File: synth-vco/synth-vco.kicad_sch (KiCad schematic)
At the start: 146 parts, among them J1 Conn_Coaxial, J2 Screw_Terminal_01x10, J3 Screw_Terminal_01x05, J4 Conn_Coaxial, J5 Barrel_Jack, U1 ADF4158, U10 LT3045IMSE_TRPBF, U11 LT3045IMSE_TRPBF, U12 LT3045IMSE_TRPBF, U13 LT8570EMS8E_TRPBF, U14 LT3065EDDPBF, U15 LT3065EDDPBF, U16 BT09E, U3 ADP-2-10+, U4 DAT-15R5A-SP+, U5 OPA192IDGKT, U6 TPSM53602RDAR, U7 LT3045IMSE_TRPBF, U8 LT3045IMSE_TRPBF, U9 LT3045IMSE_TRPBF, Y3 CVCO55CW-0500-1000

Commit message: fix: resistors, capacitors and inductors footprints
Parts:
- C1, C12, C13, C14, C15, C16, C17, C2, C20, C21, C22, C4, C5, C66, C67, C68, C69, C71, C72: footprint (none) -> Capacitor_SMD:C_0603_1608Metric_Pad1.08x0.95mm_HandSolder
- C23, C24, C29, C30, C31, C32, C33, C34, C35, C36, C38, C39, C41, C42, C44: footprint Capacitor_SMD:C_0603_1608Metric_Pad1.08x0.95mm_HandSolder -> Capacitor_SMD:C_0805_2012Metric_Pad1.18x1.45mm_HandSolder
- C25, C26, C27, C28, C49, C51, C55, C65: footprint Capacitor_SMD:C_0603_1608Metric_Pad1.08x0.95mm_HandSolder -> Capacitor_SMD:C_1206_3216Metric_Pad1.33x1.80mm_HandSolder
- C56: footprint Capacitor_SMD:C_0201_0603Metric_Pad0.64x0.40mm_HandSolder -> Capacitor_SMD:C_0603_1608Metric_Pad1.08x0.95mm_HandSolder
- C6, C7: footprint Capacitor_SMD:C_0201_0603Metric_Pad0.64x0.40mm_HandSolder -> Capacitor_SMD:C_1206_3216Metric_Pad1.33x1.80mm_HandSolder
- C70: footprint (none) -> Capacitor_SMD:C_0805_2012Metric_Pad1.18x1.45mm_HandSolder
- C9: footprint (none) -> Capacitor_SMD:C_1206_3216Metric_Pad1.33x1.80mm_HandSolder
- L1, L3, L4, L5, L6: footprint Inductor_SMD:L_0201_0603Metric_Pad0.64x0.40mm_HandSolder -> Inductor_SMD:L_0603_1608Metric_Pad1.05x0.95mm_HandSolder
- R1, R2, R22, R23, R24, R25, R26, R27, R28, R29, R30, R31, R32, R33, R34, R35, R36, R37, R38, R4: footprint Resistor_SMD:R_0201_0603Metric_Pad0.64x0.40mm_HandSolder -> Resistor_SMD:R_0603_1608Metric_Pad0.98x0.95mm_HandSolder
- R10, R11, R12, R13, R14, R15, R16, R17, R18, R19, R20, R21, R3, R39, R40, R41, R5, R6, R8, R9: footprint Resistor_SMD:R_01005_0402Metric_Pad0.57x0.30mm_HandSolder -> Resistor_SMD:R_0603_1608Metric_Pad0.98x0.95mm_HandSolder
- R7: footprint (none) -> Resistor_SMD:R_0603_1608Metric_Pad0.98x0.95mm_HandSolder

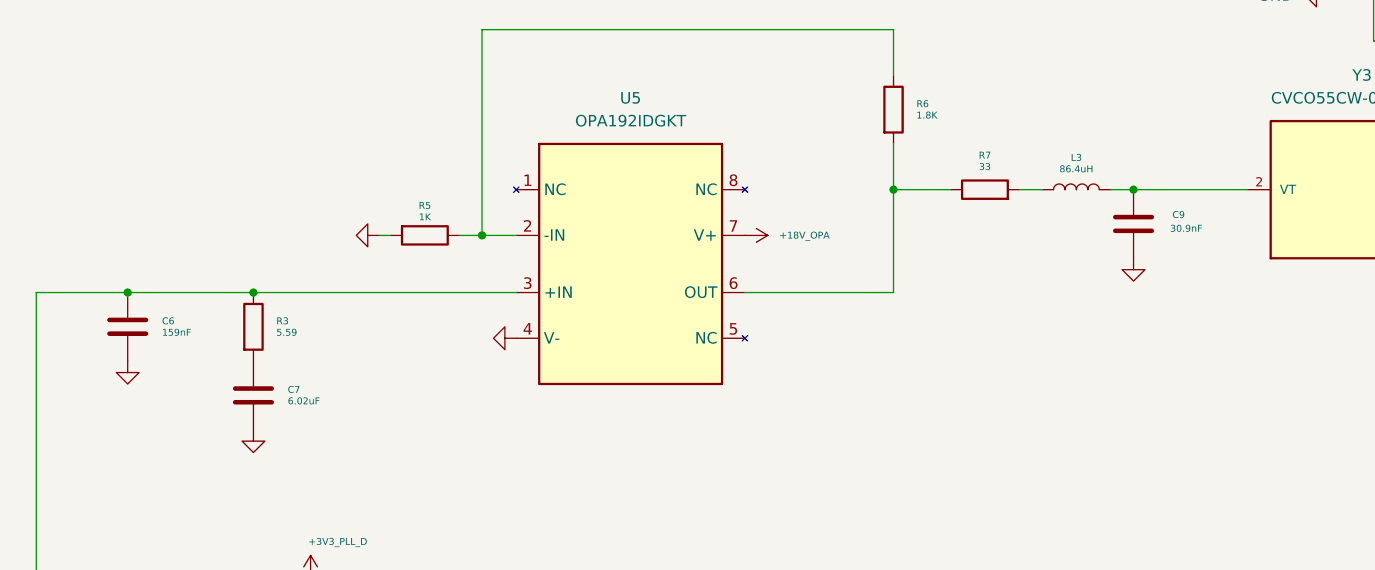
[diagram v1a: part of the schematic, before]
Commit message: refactor: standard values for adf-vco loop components
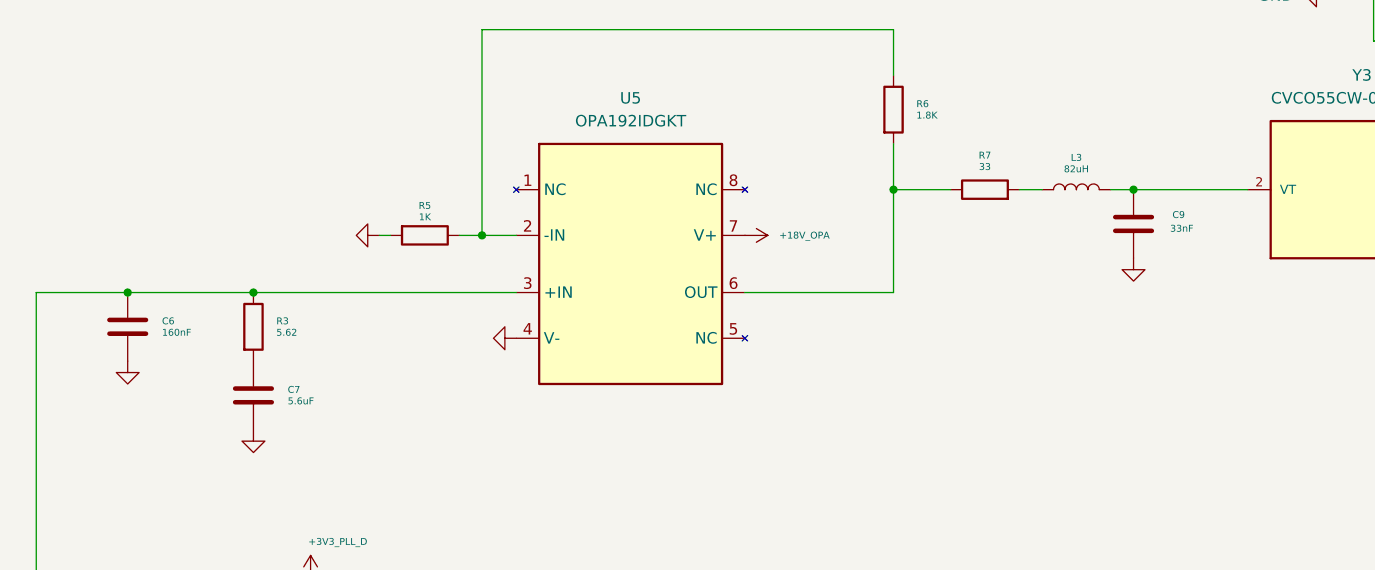
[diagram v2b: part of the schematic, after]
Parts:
- C6: value 159nF -> 160nF
- C7: value 6.02uF -> 5.6uF
- C9: value 30.9nF -> 33nF
- L3: value 86.4uH -> 82uH
- R3: value 5.59 -> 5.62
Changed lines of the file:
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@@
 			)
 		)
-		(property "Value" "30.9nF"
+		(property "Value" "33nF"
 			(at 334.264 324.358 0)
 			(show_name no)
@@
 			)
 		)
-		(property "Value" "6.02uF"
+		(property "Value" "5.6uF"
 			(at 236.22 343.535 0)
 			(show_name no)
@@
 			)
 		)
-		(property "Value" "86.4uH"
+		(property "Value" "82uH"
 			(at 323.85 317.754 90)
 			(show_name no)
@@
 			)
 		)
-		(property "Value" "5.59"
+		(property "Value" "5.62"
 			(at 234.95 335.915 0)
 			(show_name no)
@@
 			)
 		)
-		(property "Value" "159nF"
+		(property "Value" "160nF"
 			(at 222.25 335.915 0)
 			(show_name no)

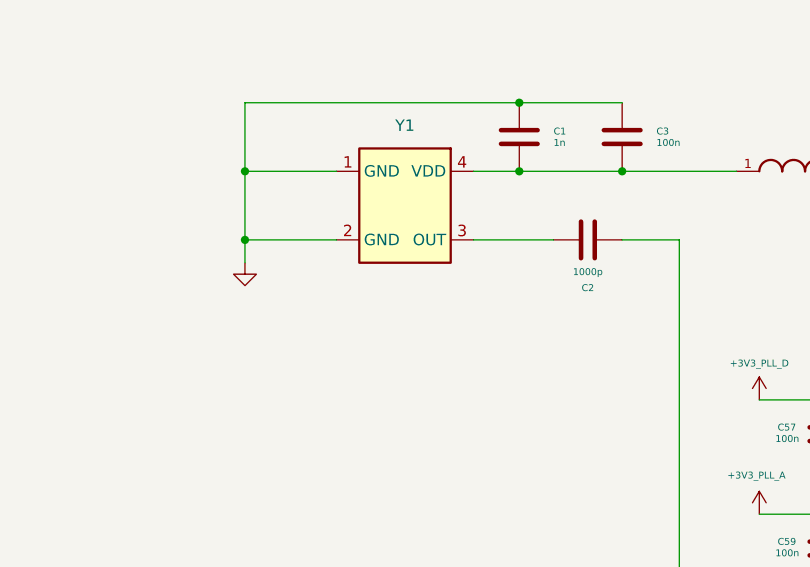
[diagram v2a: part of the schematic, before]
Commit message: fix: added value field for ft3mn
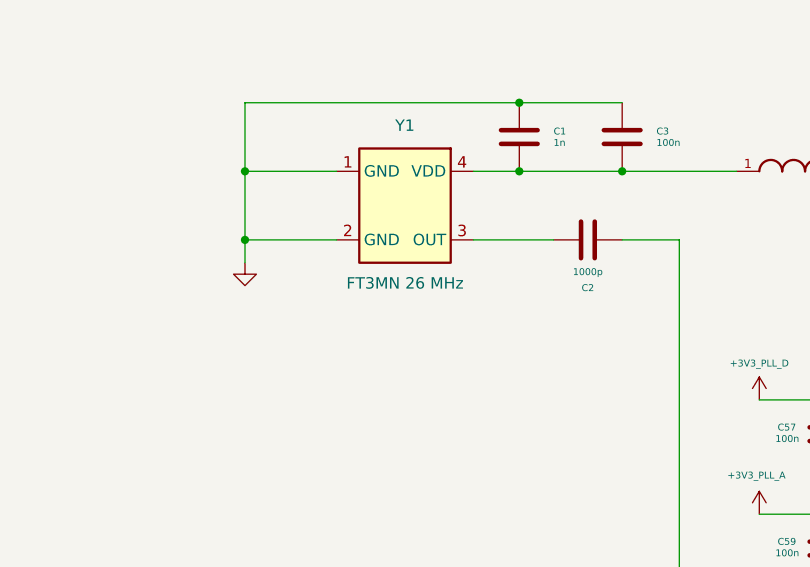
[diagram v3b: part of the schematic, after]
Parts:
- Y1: value (none) -> FT3MN 26 MHz
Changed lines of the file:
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@@
 		(in_pos_files yes)
 		(dnp no)
-		(fields_autoplaced yes)
 		(property "Reference" "Y1"
 			(at 110.49 299.72 90)
@@
 			)
 		)
-		(property "Value" ""
-			(at 110.49 308.61 0)
+		(property "Value" "FT3MN 26 MHz"
+			(at 110.49 317.246 90)
 			(show_name no)
 			(do_not_autoplace no)

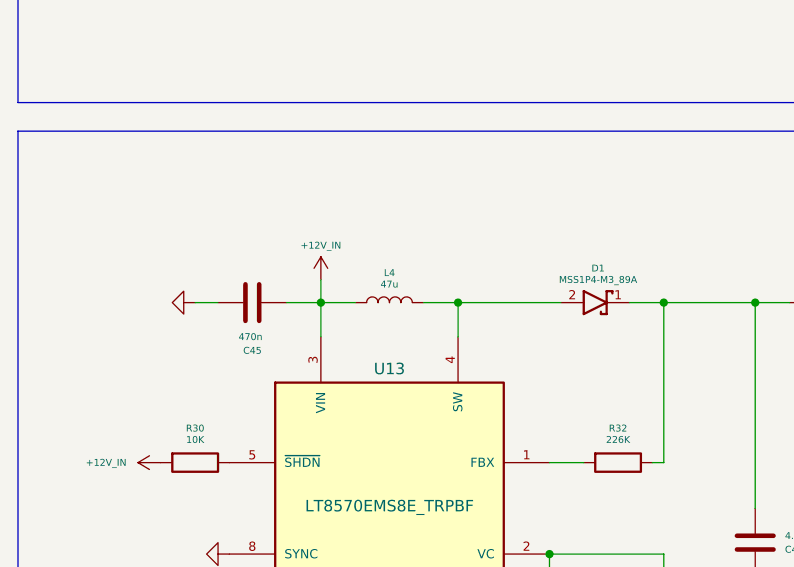
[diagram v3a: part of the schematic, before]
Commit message: fix: switched the regular boost inductor for wurth's LQS-4018
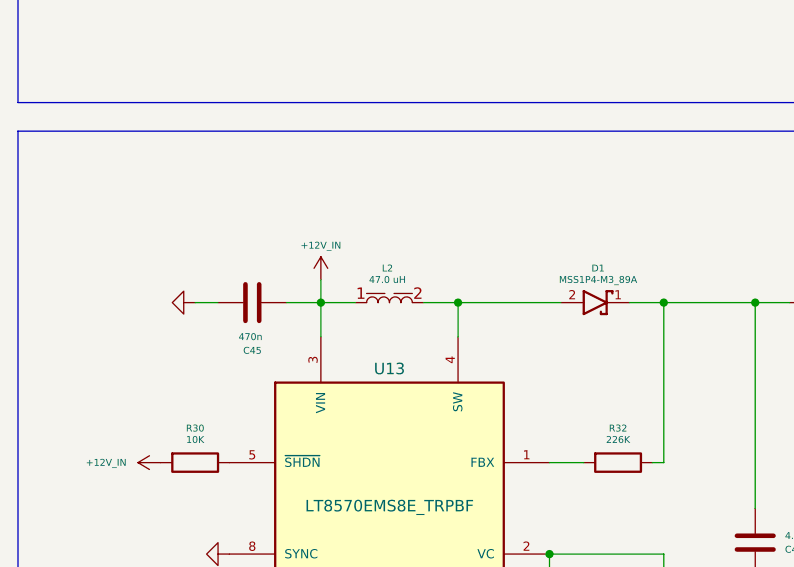
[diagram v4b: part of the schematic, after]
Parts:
- removed L4: 47u, Inductor_SMD:L_0603_1608Metric_Pad1.05x0.95mm_HandSolder, symbol Device:L
- added L2: 47.0 uH, GPR_Radar_Footprints:L_Wurth_WE-LQS-4018, symbol Inductor_Wurth_WE-LQS:4018_74404042470
- L3: footprint Inductor_SMD:L_0603_1608Metric_Pad1.05x0.95mm_HandSolder -> Inductor_SMD:L_0805_2012Metric_Pad1.05x1.20mm_HandSolder
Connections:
- net +12V_IN: now also L2.1
- net at D1.2, U13.4 (SW): now also L2.2
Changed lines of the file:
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@@
 	)
 	(symbol
-		(lib_id "Device:L")
-		(at 69.85 138.43 90)
-		(unit 1)
-		(body_style 1)
-		(exclude_from_sim no)
-		(in_bom yes)
-		(on_board yes)
-		(in_pos_files yes)
-		(dnp no)
-		(property "Reference" "L4"
-			(at 69.85 135.128 90)
-			(show_name no)
-			(do_not_autoplace no)
-			(effects
-				(font
-					(size 0.762 0.762)
-				)
-			)
-		)
-		(property "Value" "47u"
-			(at 69.85 136.398 90)
-			(show_name no)
-			(do_not_autoplace no)
-			(effects
-				(font
-					(size 0.762 0.762)
-				)
-			)
-		)
-		(property "Footprint" "Inductor_SMD:L_0603_1608Metric_Pad1.05x0.95mm_HandSolder"
-			(at 69.85 138.43 0)
-			(hide yes)
-			(show_name no)
-			(do_not_autoplace no)
-			(effects
-				(font
-					(size 1.27 1.27)
-				)
-			)
-		)
-		(property "Datasheet" ""
-			(at 69.85 138.43 0)
-			(hide yes)
-			(show_name no)
-			(do_not_autoplace no)
-			(effects
-				(font
-					(size 1.27 1.27)
-				)
-			)
-		)
-		(property "Description" "Inductor"
-			(at 69.85 138.43 0)
-			(hide yes)
-			(show_name no)
-			(do_not_autoplace no)
-			(effects
-				(font
-					(size 1.27 1.27)
-				)
-			)
-		)
-		(pin "2"
-		)
-		(pin "1"
-		)
-		(instances
-			(project "synth-vco"
-				(path "/73cd0915-f93d-4399-bfe5-6d917fa8cde7"
-					(reference "L4")
-					(unit 1)
-				)
-			)
-		)
-	)
-	(symbol
 		(lib_id "power:GND")
 		(at 52.07 166.37 270)
@@
 			)
 		)
-		(property "Footprint" "Inductor_SMD:L_0603_1608Metric_Pad1.05x0.95mm_HandSolder"
+		(property "Footprint" "Inductor_SMD:L_0805_2012Metric_Pad1.05x1.20mm_HandSolder"
 			(at 323.85 320.04 0)
 			(hide yes)
@@
 					(unit 1)
 				)
+			)
+		)
+	)
+	(symbol
+		(lib_id "Inductor_Wurth_WE-LQS:4018_74404042470")
+		(at 69.85 138.43 0)
+		(unit 1)
+		(body_style 1)
+		(exclude_from_sim no)
+		(in_bom yes)
+		(on_board yes)
+		(in_pos_files yes)
+		(dnp no)
+		(fields_autoplaced yes)
+		(property "Reference" "L2"
+			(at 69.6277 134.62 0)
+			(show_name no)
+			(do_not_autoplace no)
+			(effects
+				(font
+					(size 0.762 0.762)
+				)
+			)
+		)
+		(property "Value" "47.0 uH"
+			(at 82.55 115.57 0)
+			(hide yes)
+			(show_name no)
+			(do_not_autoplace no)
+			(effects
+				(font
+					(size 1.27 1.27)
+				)
+				(justify left)
+			)
+		)
+		(property "Footprint" "GPR_Radar_Footprints:L_Wurth_WE-LQS-4018"
+			(at 82.55 118.11 0)
+			(hide yes)
+			(show_name no)
+			(do_not_autoplace no)
+			(effects
+				(font
+					(size 1.27 1.27)
+				)
+				(justify left)
+			)
+		)
+		(property "Datasheet" "https://www.we-online.com/catalog/datasheet/74404042470.pdf?ki"
+			(at 82.55 120.65 0)
+			(hide yes)
+			(show_name no)
+			(do_not_autoplace no)
+			(effects
+				(font
+					(size 1.27 1.27)
+				)
+				(justify left)
+			)
+		)
+		(property "Description" "SMT Power Inductor"
+			(at 69.85 138.43 0)
+			(hide yes)
+			(show_name no)
+			(do_not_autoplace no)
+			(effects
+				(font
+					(size 1.27 1.27)
+				)
+			)
+		)
+		(property "Manufacturer" "Wurth Elektronik"
+			(at 82.55 123.19 0)
+			(hide yes)
+			(show_name no)
+			(do_not_autoplace no)
+			(effects
+				(font
+					(size 1.27 1.27)
+				)
+				(justify left)
+			)
+		)
+		(property "Manufacturer URL" "https://www.we-online.com"
+			(at 82.55 125.73 0)
+			(hide yes)
+			(show_name no)
+			(do_not_autoplace no)
+			(effects
+				(font
+					(size 1.27 1.27)
+				)
+				(justify left)
+			)
+		)
+		(property "Created Date" "20251218"
+			(at 82.55 128.27 0)
+			(hide yes)
+			(show_name no)
+			(do_not_autoplace no)
+			(effects
+				(font
+					(size 1.27 1.27)
+				)
+				(justify left)
+			)
+		)
+		(property "Series" "WE-LQS"
+			(at 82.55 130.81 0)
+			(hide yes)
+			(show_name no)
+			(do_not_autoplace no)
+			(effects
+				(font
+					(size 1.27 1.27)
+				)
+				(justify left)
+			)
+		)
+		(property "Part Number" "74404042470"
+			(at 82.55 133.35 0)
+			(hide yes)
+			(show_name no)
+			(do_not_autoplace no)
+			(effects
+				(font
+					(size 1.27 1.27)
+				)
+				(justify left)
+			)
+		)
+		(property "Size" "4018"
+			(at 82.55 135.89 0)
+			(hide yes)
+			(show_name no)
+			(do_not_autoplace no)
+			(effects
+				(font
+					(size 1.27 1.27)
+				)
+				(justify left)
+			)
+		)
+		(property "Mounting Technology" "SMT"
+			(at 82.55 138.43 0)
+			(hide yes)
+			(show_name no)
+			(do_not_autoplace no)
+			(effects
+				(font
+					(size 1.27 1.27)
+				)
+				(justify left)
+			)
+		)
+		(property "L (uH)" "47.0"
+			(at 82.55 140.97 0)
+			(hide yes)
+			(show_name no)
+			(do_not_autoplace no)
+			(effects
+				(font
+					(size 1.27 1.27)
+				)
+				(justify left)
+			)
+		)
+		(property "IR (A)" "0.6"
+			(at 82.55 143.51 0)
+			(hide yes)
+			(show_name no)
+			(do_not_autoplace no)
+			(effects
+				(font
+					(size 1.27 1.27)
+				)
+				(justify left)
+			)
+		)
+		(property "ISAT (A)" "0.7"
+			(at 82.55 146.05 0)
+			(hide yes)
+			(show_name no)
+			(do_not_autoplace no)
+			(effects
+				(font
+					(size 1.27 1.27)
+				)
+				(justify left)
+			)
+		)
+		(property "RDC (mohm)" "620"
+			(at 82.55 148.59 0)
+			(hide yes)
+			(show_name no)
+			(do_not_autoplace no)
+			(effects
+				(font
+					(size 1.27 1.27)
+				)
+				(justify left)
+			)
+		)
+		(property "fres (MHz)" "11.0"
+			(at 82.55 151.13 0)
+			(hide yes)
+			(show_name no)
+			(do_not_autoplace no)
+			(effects
+				(font
+					(size 1.27 1.27)
+				)
+				(justify left)
+			)
+		)
+		(property "Critical Parameter" "47.0 uH"
+			(at 69.6277 135.89 0)
+			(show_name no)
+			(do_not_autoplace no)
+			(effects
+				(font
+					(size 0.762 0.762)
+				)
+			)
+		)
+		(pin "2"
+		)
+		(pin "1"
+		)
+		(instances
+			(project "synth-vco"
+				(path "/73cd0915-f93d-4399-bfe5-6d917fa8cde7"
+					(reference "L2")
+					(unit 1)
+				)

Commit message: fix: erc errors
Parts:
- FL1, FL2: footprint BLM18EG331TZ1D:BEADC1608X65N -> GPR_Radar_Footprints:BEADC1608X65N
- U5: footprint OPA192IDGKT:SOP65P490X110-8N -> GPR_Radar_Footprints:SOP65P490X110-8N
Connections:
- no-connect marks 10 -> 12
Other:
- moved on the sheet: FL2
